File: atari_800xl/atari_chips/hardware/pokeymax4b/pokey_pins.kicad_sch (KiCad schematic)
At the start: 5 parts, among them J1 Conn_02x02_Odd_Even, J3 Conn_02x05_Odd_Even

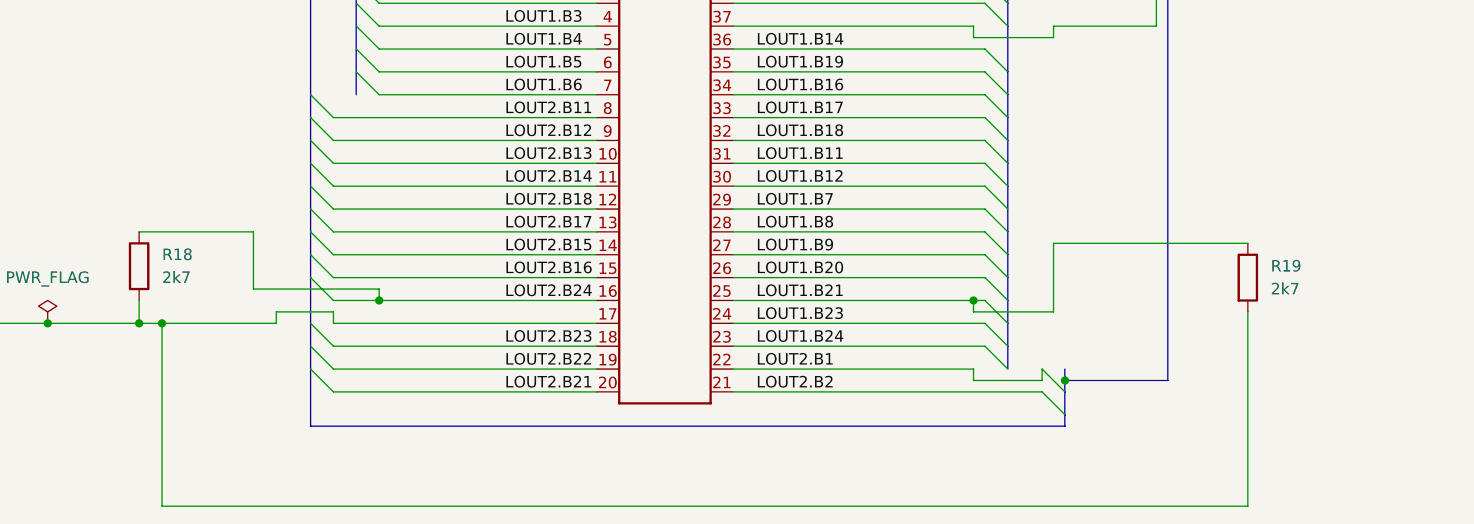
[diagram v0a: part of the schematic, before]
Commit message: After testing 4b first run, there are a few issues. Updated to 4b2 with: Corrected L/R output. ADC bias improvement. ADC preamp out/in- corrected. Moved silkscreen name!
git-svn-id: svn+ssh://192.168.0.3/home/svnfpga/repo/trunk@1475 d6161ac3-aae1-4d52-9b05-ea9ac36b53d3
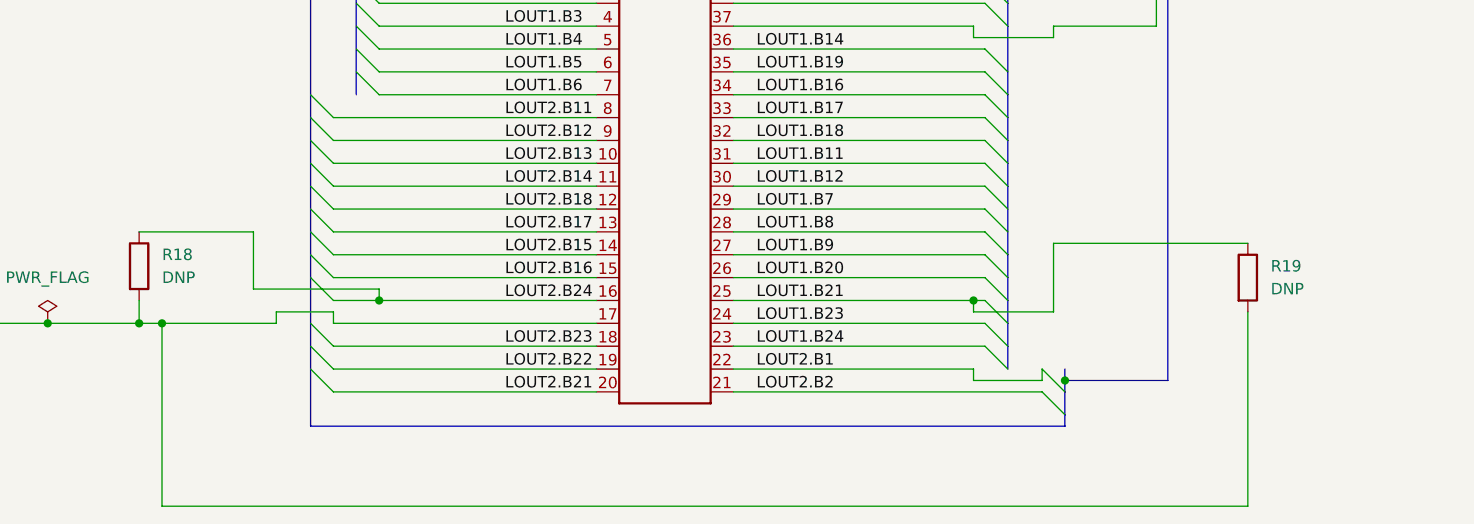
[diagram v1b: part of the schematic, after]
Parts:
- R18, R19: value 2k7 -> DNP
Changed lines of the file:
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@@
 			)
 		)
-		(property "Value" "2k7"
+		(property "Value" "DNP"
 			(at 46.99 116.8399 0)
 			(effects
@@
 			)
 		)
-		(property "Value" "2k7"
+		(property "Value" "DNP"
 			(at 170.18 118.1099 0)
 			(effects
